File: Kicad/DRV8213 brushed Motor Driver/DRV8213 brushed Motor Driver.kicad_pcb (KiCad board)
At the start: 4 copper layers, 15 x 15 mm, 26 parts, among them J1 Keystone 3569, J10 1.27mm pin header, J11 1.27mm pin header, J2 Keystone 3579, J3 Keystone 3579, J4 Keystone 3569, J5 Keystone 3569, J6 Keystone 3579, J7 Keystone 3579, J8 Keystone 3569, J9 JST PH 2mm horizontal, U1 DRV8213RTER, U2 LP2981-3.3

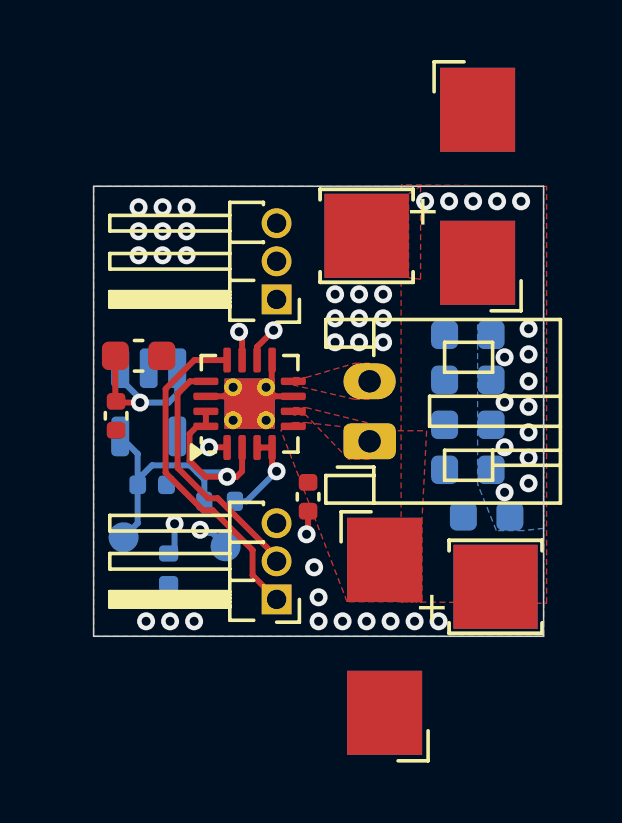
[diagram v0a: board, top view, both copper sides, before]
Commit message: Fixed routing of DRV8213 board and updated 3d models
I swapped the current sense and the PWM input headers accidentally! I fixed that now. I also added the proper 3d models and footprints. I exported a 3d model of the board. The last change I made ws cleaning up the inner layers to only be power planes.
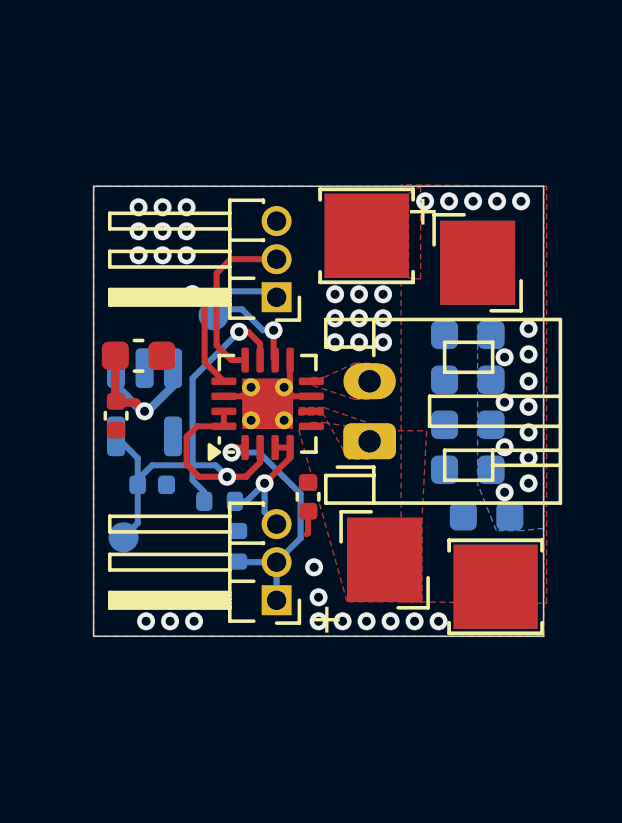
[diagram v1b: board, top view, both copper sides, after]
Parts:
- J1, J4, J5, J8: footprint custom_Connector:Keystone_3569 -> custom_Connector:Keystone_3569_half
- moved J10 10.1 mm to (169.9, 97.9)
- moved J11 10.0 mm to (169.9, 108.0)
- moved TP1 7.71 mm to (167.8, 98.5)
- moved R2 2.42 mm to (168.6, 106.2), turned to 90 degrees
- moved U1 0.60 mm to (169.6, 101.5)
- moved U2 0.14 mm to (165.5, 101.4)
- turned J1 to 180 degrees
- turned J5 to 0 degrees
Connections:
- U1 pad 12: Net-(J10-Pin_1) -> Net-(J10-Pin_2)
- U1 pad 13: Net-(J10-Pin_2) -> Net-(J10-Pin_1)
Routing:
- net /Fault: track 12.6 -> 4.81 mm
- net Net-(U1-TINRUSH): track 10.7 -> 3.39 mm, vias 2 -> 1
- net /CSA-A: track 13.6 -> 8.68 mm, vias 2 -> 1
- net Net-(J10-Pin_1): track 11.2 -> 6.27 mm, vias 0 -> 1
- net Net-(J10-Pin_2): track 8.26 -> 5.75 mm
- net +3.3V: track 19.7 -> 21.4 mm
- net GNDPWR: vias 30 -> 29

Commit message: Fixed headers and connectors miss-alignments
Almost everything was misaligned. The holes on the hub to hub headers must be 2.9mm from the edge, the header holes on the motor drivers must be 4.5mm from the edge, and the centers of the power connectors(either gender) must be 2.15mm from the edge
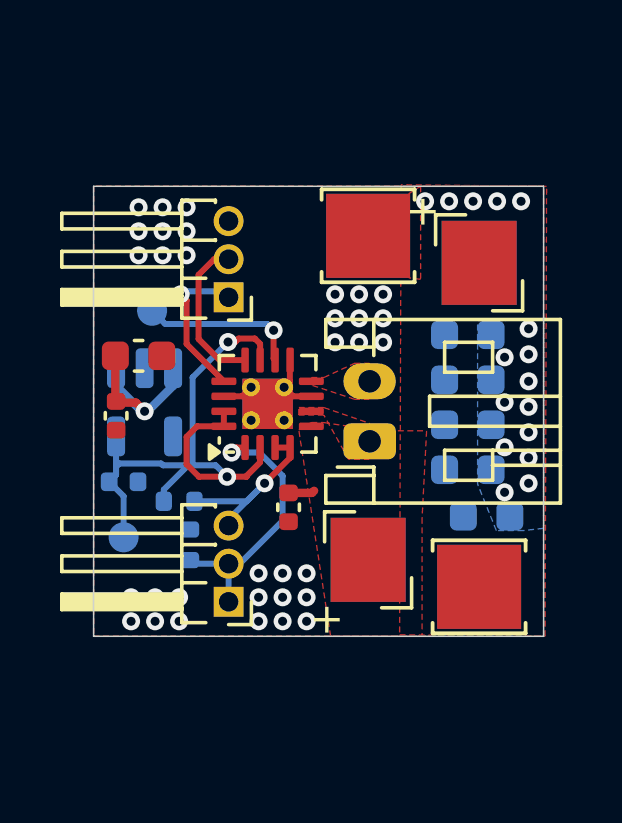
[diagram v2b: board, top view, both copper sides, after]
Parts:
- moved TP1 2.06 mm to (165.8, 98.3)
- moved J11 1.60 mm to (168.3, 108.0)
- moved R2 1.60 mm to (167.0, 106.2)
- moved J10 1.60 mm to (168.3, 97.9)
- moved R1 1.35 mm to (166.7, 104.7)
- moved C9 0.96 mm to (164.8, 104.0)
- moved C6 0.74 mm to (170.3, 104.9)
- moved J3 0.55 mm to (176.7, 107.5)
- moved J1 0.55 mm to (172.9, 109.2)
- moved J5 0.55 mm to (172.9, 109.2)
- moved J7 0.55 mm to (176.7, 107.5)
- moved J2 0.05 mm to (172.9, 95.8)
- moved J4 0.05 mm to (176.7, 94.2)
- moved J8 0.05 mm to (176.7, 94.2)
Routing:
- net Net-(U1-TINRUSH): track 3.39 -> 5.33 mm
- net /Fault: track 4.81 -> 6.54 mm
- net Net-(J10-Pin_1): track 6.27 -> 5.22 mm
- net VDD: track 6.54 -> 7.42 mm
- net GNDPWR: track 3.85 -> 3.06 mm, vias 29 -> 33
- net Net-(J10-Pin_2): track 5.75 -> 5.20 mm

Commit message: Added LCSC part numbers, DNP attr, and exported Gerbers
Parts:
- C6, C8: value 0.1uF, 16v -> 100nF, 16v
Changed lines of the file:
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@@
 			)
 		)
-		(property "Value" "0.1uF, 16v"
+		(property "Value" "100nF, 16v"
 			(at 0 1.16 90)
 			(layer "F.Fab")
@@
 			)
 		)
+		(property "LCSC" "C1525"
+			(at 0 0 0)
+			(layer "F.SilkS")
+			(hide yes)
+			(effects
+				(font
+					(size 1.27 1.27)
+					(thickness 0.15)
+				)
+			)
+		)
 		(property ki_fp_filters "C_*")
 		(sheetname "Root")
@@
 			)
 		)
+		(property "LCSC" "C96446"
+			(at 0 0 0)
+			(layer "F.SilkS")
+			(hide yes)
+			(effects
+				(font
+					(size 1.27 1.27)
+					(thickness 0.15)
+				)
+			)
+		)
 		(property ki_fp_filters "C_*")
 		(sheetname "Root")
@@
 			)
 		)
+		(property "LCSC" "C295747"
+			(at 0 0 0)
+			(layer "F.SilkS")
+			(hide yes)
+			(effects
+				(font
+					(size 1.27 1.27)
+					(thickness 0.15)
+				)
+			)
+		)
 		(property ki_fp_filters "Connector*:*_1x??_*")
 		(sheetname "Root")
@@
 		(sheetname "Root")
 		(sheetfile "DRV8213 brushed Motor Driver.kicad_sch")
-		(attr smd)
+		(attr smd dnp)
 		(fp_line
 			(start 1.61 -1.61)
@@
 			)
 		)
-		(property "Value" "0.1uF, 16v"
+		(property "Value" "100nF, 16v"
 			(at 0 1.16 -90)
 			(layer "F.Fab")
@@
 			)
 		)
+		(property "LCSC" "C1525"
+			(at 0 0 0)
+			(layer "F.SilkS")
+			(hide yes)
+			(effects
+				(font
+					(size 1.27 1.27)
+					(thickness 0.15)
+				)
+			)
+		)
 		(property ki_fp_filters "C_*")
 		(sheetname "Root")
@@
 			)
 		)
+		(property "LCSC" "C96446"
+			(at 0 0 0)
+			(layer "B.SilkS")
+			(hide yes)
+			(effects
+				(font
+					(size 1.27 1.27)
+					(thickness 0.15)
+				)
+			)
+		)
 		(property ki_fp_filters "C_*")
 		(sheetname "Root")
@@
 			)
 		)
+		(property "LCSC" "C96446"
+			(at 0 0 0)
+			(layer "B.SilkS")
+			(hide yes)
+			(effects
+				(font
+					(size 1.27 1.27)
+					(thickness 0.15)
+				)
+			)
+		)
 		(property ki_fp_filters "C_*")
 		(sheetname "Root")
@@
 			)
 		)
+		(property "LCSC" "C96446"
+			(at 0 0 0)
+			(layer "B.SilkS")
+			(hide yes)
+			(effects
+				(font
+					(size 1.27 1.27)
+					(thickness 0.15)
+				)
+			)
+		)
 		(property ki_fp_filters "C_*")
 		(sheetname "Root")
@@
 			)
 		)
+		(property "LCSC" "C96446"
+			(at 0 0 0)
+			(layer "B.SilkS")
+			(hide yes)
+			(effects
+				(font
+					(size 1.27 1.27)
+					(thickness 0.15)
+				)
+			)
+		)
 		(property ki_fp_filters "C_*")
 		(sheetname "Root")
@@
 			)
 		)
+		(property "LCSC" "C12530"
+			(at 0 0 0)
+			(layer "B.SilkS")
+			(hide yes)
+			(effects
+				(font
+					(size 1.27 1.27)
+					(thickness 0.15)
+				)
+			)
+		)
 		(property ki_fp_filters "C_*")
 		(sheetname "Root")
@@
 			)
 		)
+		(property "LCSC" "C25890"
+			(at 0 0 0)
+			(layer "B.SilkS")
+			(hide yes)
+			(effects
+				(font
+					(size 1.27 1.27)
+					(thickness 0.15)
+				)
+			)
+		)
 		(property ki_fp_filters "R_*")
 		(sheetname "Root")
@@
 			)
 		)
+		(property "LCSC" "C129997"
+			(at 0 0 0)
+			(layer "B.SilkS")
+			(hide yes)
+			(effects
+				(font
+					(size 1.27 1.27)
+					(thickness 0.15)
+				)
+			)
+		)
 		(property ki_fp_filters "SOT?23*")
 		(sheetname "Root")
@@
 			)
 		)
+		(property "LCSC" "C25744"
+			(at 0 0 0)
+			(layer "B.SilkS")
+			(hide yes)
+			(effects
+				(font
+					(size 1.27 1.27)
+					(thickness 0.15)
+				)
+			)
+		)
 		(property ki_fp_filters "R_*")
 		(sheetname "Root")
@@
 			)
 		)
+		(property "LCSC" "C96446"
+			(at 0 0 0)
+			(layer "B.SilkS")
+			(hide yes)
+			(effects
+				(font
+					(size 1.27 1.27)
+					(thickness 0.15)
+				)
+			)
+		)
